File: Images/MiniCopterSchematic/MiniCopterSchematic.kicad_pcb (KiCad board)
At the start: 2 copper layers, 17 parts, among them M1 MOTOR_DC_1, M2 MOTOR_DC_2, M3 MOTOR_DC_3, M4 MOTOR_DC_4, Q1 FQP20NO6L, Q2 FQP20NO6L, Q3 FQP20NO6L, Q4 FQP20NO6L

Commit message: Working on PCB layout/wiring
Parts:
- added H1: MountingHole, MountingHole:MountingHole_3.2mm_M3, F.Cu at (166.4, 119.4)
- added H2: MountingHole, MountingHole:MountingHole_3.2mm_M3, F.Cu at (158.4, 111.4)
- added H3: MountingHole, MountingHole:MountingHole_3.2mm_M3, F.Cu at (158.4, 119.4)
- added H4: MountingHole, MountingHole:MountingHole_3.2mm_M3, F.Cu at (166.4, 111.4)
- IMU1: footprint Connector_PinSocket_2.54mm:PinSocket_1x07_P2.54mm_Vertical -> AA_Custom_Components:MPU6050
- moved M1 26.7 mm to (86.2, 123.8), turned to 0 degrees
- moved M4 17.8 mm to (97.0, 81.3), turned to 0 degrees
- moved LIPO_BATTERY_1 15.6 mm to (80.0, 92.2)
- moved Q1 14.9 mm to (97.7, 111.9)
- moved Q2 14.6 mm to (97.7, 116.7)
- moved M3 14.3 mm to (117.9, 81.3)
- moved LIPO_BATTERY_2 13.4 mm to (80.0, 110.6), turned to -90 degrees
- moved R3 12.3 mm to (113.0, 116.8)
- moved R4 12.3 mm to (113.0, 120.0)
- moved A1 11.7 mm to (110.2, 88.9)
- moved R1 11.1 mm to (113.0, 101.6)
- moved R2 11.1 mm to (113.0, 106.1)
- moved Q4 10.4 mm to (97.6, 126.5)
- moved IMU1 10.3 mm to (101.7, 87.7), turned to -90 degrees
- moved Q3 9.34 mm to (97.7, 121.5)
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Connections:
- IMU1 pad 1: unconnected-(IMU1-Pad1) -> +BATT
- IMU1 pad 2: unconnected-(IMU1-Pad2) -> GND
- IMU1 pad 3: SDA -> SCL
- IMU1 pad 4: SCL -> SDA
- IMU1 pad 6: GND -> unconnected-(IMU1-Pad6)
- IMU1 pad 7: +BATT -> unconnected-(IMU1-Pad7)
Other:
- board outline added: 76.2 x 55.9 mm

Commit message: Working on PCB
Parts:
- H1, H2, H3, H4: footprint MountingHole:MountingHole_3.2mm_M3 -> MountingHole:MountingHole_3.2mm_M3_Pad
- moved H1 95.6 mm to (78.7, 81.3)
- moved H3 80.0 mm to (78.7, 127.0)
- moved H2 32.1 mm to (145.4, 82.1)
- moved H4 26.6 mm to (144.8, 127.0)
- moved Q4 13.2 mm to (88.8, 116.7)
- moved Q3 13.2 mm to (88.9, 111.8)
- moved M1 8.91 mm to (95.1, 124.5)
- moved LIPO_BATTERY_1 1.91 mm to (80.0, 94.1)
- moved Q1 1.37 mm to (99.1, 111.8)
- moved Q2 1.37 mm to (99.1, 116.6)
- moved LIPO_BATTERY_2 1.27 mm to (80.0, 111.8)
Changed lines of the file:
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@@
   (net 36 "unconnected-(NRF24L01_1-Pad8)")
   (net 37 "unconnected-(IMU1-Pad8)")
-  (footprint "MountingHole:MountingHole_3.2mm_M3" (layer "F.Cu")
-    (at 166.37 119.38)
-    (descr "Mounting Hole 3.2mm, no annular, M3")
-    (tags "mounting hole 3.2mm no annular m3")
+  (footprint "MountingHole:MountingHole_3.2mm_M3_Pad" (layer "F.Cu")
+    (at 78.74 81.28)
+    (descr "Mounting Hole 3.2mm, M3")
+    (tags "mounting hole 3.2mm m3")
     (property "Sheetfile" "MiniCopterSchematic.kicad_sch")
     (property "Sheetname" "")
@@
     (fp_circle (center 0 0) (end 3.2 0) (layer "Cmts.User") (width 0.15) (fill none))
     (fp_circle (center 0 0) (end 3.45 0) (layer "F.CrtYd") (width 0.05) (fill none))
-    (pad "" np_thru_hole circle (at 0 0) (size 3.2 3.2) (drill 3.2) (layers *.Cu *.Mask))
+    (pad "1" thru_hole circle (at 0 0) (size 6.4 6.4) (drill 3.2) (layers *.Cu *.Mask))
   )
   (footprint "Connector_PinSocket_2.54mm:PinSocket_1x03_P2.54mm_Vertical" (layer "F.Cu")
-    (at 97.7095 121.532 90)
+    (at 88.9 111.76 90)
     (descr "Through hole straight socket strip, 1x03, 2.54mm pitch, single row (from Kicad 4.0.7), script generated")
     (tags "Through hole socket strip THT 1x03 2.54mm single row")
@@
   )
   (footprint "AA_Custom_Components:PowerPad_Pair_5.0x5.0mm" (layer "F.Cu")
-    (at 80.01 110.57 -90)
+    (at 80.01 111.84 -90)
     (descr "SMD rectangular pad as solderable power pads, square 5.0mm side length each")
     (tags "SMD pad rectangle square power")
@@
       (net 35 "Net-(M4-Pad2)") (pinfunction "-") (pintype "passive"))
   )
-  (footprint "MountingHole:MountingHole_3.2mm_M3" (layer "F.Cu")
-    (at 158.42 111.43)
-    (descr "Mounting Hole 3.2mm, no annular, M3")
-    (tags "mounting hole 3.2mm no annular m3")
+  (footprint "MountingHole:MountingHole_3.2mm_M3_Pad" (layer "F.Cu")
+    (at 145.43 82.09)
+    (descr "Mounting Hole 3.2mm, M3")
+    (tags "mounting hole 3.2mm m3")
     (property "Sheetfile" "MiniCopterSchematic.kicad_sch")
     (property "Sheetname" "")
@@
     (fp_circle (center 0 0) (end 3.2 0) (layer "Cmts.User") (width 0.15) (fill none))
     (fp_circle (center 0 0) (end 3.45 0) (layer "F.CrtYd") (width 0.05) (fill none))
-    (pad "" np_thru_hole circle (at 0 0) (size 3.2 3.2) (drill 3.2) (layers *.Cu *.Mask))
+    (pad "1" thru_hole circle (at 0 0) (size 6.4 6.4) (drill 3.2) (layers *.Cu *.Mask))
   )
   (footprint "AA_Custom_Components:PowerPad_Pair_4.0x4.0mm" (layer "F.Cu")
@@
       (net 33 "Net-(M2-Pad2)") (pinfunction "-") (pintype "passive"))
   )
-  (footprint "MountingHole:MountingHole_3.2mm_M3" (layer "F.Cu")
-    (at 166.37 111.43)
-    (descr "Mounting Hole 3.2mm, no annular, M3")
-    (tags "mounting hole 3.2mm no annular m3")
+  (footprint "MountingHole:MountingHole_3.2mm_M3_Pad" (layer "F.Cu")
+    (at 144.78 127)
+    (descr "Mounting Hole 3.2mm, M3")
+    (tags "mounting hole 3.2mm m3")
     (property "Sheetfile" "MiniCopterSchematic.kicad_sch")
     (property "Sheetname" "")
@@
     (fp_circle (center 0 0) (end 3.2 0) (layer "Cmts.User") (width 0.15) (fill none))
     (fp_circle (center 0 0) (end 3.45 0) (layer "F.CrtYd") (width 0.05) (fill none))
-    (pad "" np_thru_hole circle (at 0 0) (size 3.2 3.2) (drill 3.2) (layers *.Cu *.Mask))
+    (pad "1" thru_hole circle (at 0 0) (size 6.4 6.4) (drill 3.2) (layers *.Cu *.Mask))
   )
   (footprint "Connector_PinSocket_2.54mm:PinSocket_1x03_P2.54mm_Vertical" (layer "F.Cu")
-    (at 97.6945 111.905 90)
+    (at 99.06 111.76 90)
     (descr "Through hole straight socket strip, 1x03, 2.54mm pitch, single row (from Kicad 4.0.7), script generated")
     (tags "Through hole socket strip THT 1x03 2.54mm single row")
@@
   )
   (footprint "Connector_PinSocket_2.54mm:PinSocket_1x03_P2.54mm_Vertical" (layer "F.Cu")
-    (at 97.6945 116.731 90)
+    (at 99.06 116.586 90)
     (descr "Through hole straight socket strip, 1x03, 2.54mm pitch, single row (from Kicad 4.0.7), script generated")
     (tags "Through hole socket strip THT 1x03 2.54mm single row")
@@
   )
   (footprint "AA_Custom_Components:PowerPad_Pair_5.0x5.0mm" (layer "F.Cu")
-    (at 80.01 92.155 90)
+    (at 80.01 94.06 90)
     (descr "SMD rectangular pad as solderable power pads, square 5.0mm side length each")
     (tags "SMD pad rectangle square power")
@@
       (net 27 "+BATT") (pinfunction "-") (pintype "passive"))
   )
-  (footprint "MountingHole:MountingHole_3.2mm_M3" (layer "F.Cu")
-    (at 158.42 119.38)
-    (descr "Mounting Hole 3.2mm, no annular, M3")
-    (tags "mounting hole 3.2mm no annular m3")
+  (footprint "MountingHole:MountingHole_3.2mm_M3_Pad" (layer "F.Cu")
+    (at 78.74 127)
+    (descr "Mounting Hole 3.2mm, M3")
+    (tags "mounting hole 3.2mm m3")
     (property "Sheetfile" "MiniCopterSchematic.kicad_sch")
     (property "Sheetname" "")
@@
     (fp_circle (center 0 0) (end 3.2 0) (layer "Cmts.User") (width 0.15) (fill none))
     (fp_circle (center 0 0) (end 3.45 0) (layer "F.CrtYd") (width 0.05) (fill none))
-    (pad "" np_thru_hole circle (at 0 0) (size 3.2 3.2) (drill 3.2) (layers *.Cu *.Mask))
+    (pad "1" thru_hole circle (at 0 0) (size 6.4 6.4) (drill 3.2) (layers *.Cu *.Mask))
   )
   (footprint "Resistor_THT:R_Axial_DIN0207_L6.3mm_D2.5mm_P10.16mm_Horizontal" (layer "F.Cu")
@@
   )
   (footprint "AA_Custom_Components:PowerPad_Pair_4.0x4.0mm" (layer "F.Cu")
-    (at 86.17 123.825)
+    (at 95.06 124.46)
     (descr "SMD rectangular pad as solderable power pads, square 4.0mm side length each")
     (tags "SMD pad rectangle square power")
@@
   )
   (footprint "Connector_PinSocket_2.54mm:PinSocket_1x03_P2.54mm_Vertical" (layer "F.Cu")
-    (at 97.6425 126.461 90)
+    (at 88.833 116.689 90)
     (descr "Through hole straight socket strip, 1x03, 2.54mm pitch, single row (from Kicad 4.0.7), script generated")
     (tags "Through hole socket strip THT 1x03 2.54mm single row")

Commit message: Working on PCB
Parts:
- moved NRF24L01_1 4.07 mm to (139.8, 101.2)
- moved R1 3.76 mm to (112.6, 97.9)
- moved R2 3.76 mm to (112.6, 102.3)
- moved R3 3.76 mm to (112.6, 113.1)
- moved R4 3.15 mm to (112.7, 116.9)
- moved H2 2.11 mm to (145.7, 80.0)
- moved H1 1.28 mm to (78.7, 80.0)
- moved H4 0.96 mm to (145.7, 127.0)
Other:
- board size 76.2 x 55.9 mm -> 78.6 x 58.6 mm
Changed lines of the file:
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@@
   (net 37 "unconnected-(IMU1-Pad8)")
   (footprint "MountingHole:MountingHole_3.2mm_M3_Pad" (layer "F.Cu")
-    (at 78.74 81.28)
+    (at 78.74 80)
     (descr "Mounting Hole 3.2mm, M3")
     (tags "mounting hole 3.2mm m3")
@@
     (property "Sheetname" "")
     (attr exclude_from_pos_files)
-    (fp_text reference "H1" (at 0 -4.2) (layer "F.SilkS")
+    (fp_text reference "H1" (at 0 -4.2) (layer "F.Fab")
       (effects (font (size 1 1) (thickness 0.15)))
     )
@@
   )
   (footprint "Resistor_THT:R_Axial_DIN0207_L6.3mm_D2.5mm_P10.16mm_Horizontal" (layer "F.Cu")
-    (at 113.03 106.065)
+    (at 112.64 102.33)
     (descr "Resistor, Axial_DIN0207 series, Axial, Horizontal, pin pitch=10.16mm, 0.25W = 1/4W, length*diameter=6.3*2.5mm^2, http://cdn-reichelt.de/documents/datenblatt/B400/1_4W%23YAG.pdf")
     (tags "Resistor Axial_DIN0207 series Axial Horizontal pin pitch 10.16mm 0.25W = 1/4W length 6.3mm diameter 2.5mm")
@@
   )
   (footprint "AA_Custom_Components:NRF24L01_Breakout" (layer "F.Cu")
-    (at 139.831513 105.278487)
+    (at 139.836513 101.213487)
     (property "Sheetfile" "MiniCopterSchematic.kicad_sch")
     (property "Sheetname" "")
@@
       (effects (font (size 1 1) (thickness 0.15)))
     )
-    (fp_text value "ARDUINO NANO EVERY" (at 12.16 26.035 90) (layer "F.Fab")
+    (fp_text value "ARDUINO NANO EVERY" (at 11.83 22.9 90) (layer "F.Fab")
       (effects (font (size 1 1) (thickness 0.15)))
     )
@@
       (effects (font (size 1 1) (thickness 0.15)))
     )
-    (fp_text user "${REFERENCE}" (at 9.62 26.035 90) (layer "F.Fab")
+    (fp_text user "${REFERENCE}" (at 9.23 22.3 90) (layer "F.Fab")
       (effects (font (size 1 1) (thickness 0.15)))
     )
@@
   )
   (footprint "Resistor_THT:R_Axial_DIN0207_L6.3mm_D2.5mm_P10.16mm_Horizontal" (layer "F.Cu")
-    (at 113.03 120.015)
+    (at 112.7 116.88)
     (descr "Resistor, Axial_DIN0207 series, Axial, Horizontal, pin pitch=10.16mm, 0.25W = 1/4W, length*diameter=6.3*2.5mm^2, http://cdn-reichelt.de/documents/datenblatt/B400/1_4W%23YAG.pdf")
     (tags "Resistor Axial_DIN0207 series Axial Horizontal pin pitch 10.16mm 0.25W = 1/4W length 6.3mm diameter 2.5mm")
@@
   )
   (footprint "MountingHole:MountingHole_3.2mm_M3_Pad" (layer "F.Cu")
-    (at 145.43 82.09)
+    (at 145.74 80)
     (descr "Mounting Hole 3.2mm, M3")
     (tags "mounting hole 3.2mm m3")
@@
     (property "Sheetname" "")
     (attr exclude_from_pos_files)
-    (fp_text reference "H2" (at 0 -4.2) (layer "F.SilkS")
+    (fp_text reference "H2" (at 0 -4.2) (layer "F.Fab")
       (effects (font (size 1 1) (thickness 0.15)))
     )
@@
   )
   (footprint "MountingHole:MountingHole_3.2mm_M3_Pad" (layer "F.Cu")
-    (at 144.78 127)
+    (at 145.74 127)
     (descr "Mounting Hole 3.2mm, M3")
     (tags "mounting hole 3.2mm m3")
@@
     (property "Sheetname" "")
     (attr exclude_from_pos_files)
-    (fp_text reference "H4" (at 0 -4.2) (layer "F.SilkS")
+    (fp_text reference "H4" (at 0 -4.2) (layer "F.Fab")
       (effects (font (size 1 1) (thickness 0.15)))
     )
@@
     (property "Sheetname" "")
     (attr exclude_from_pos_files)
-    (fp_text reference "H3" (at 0 -4.2) (layer "F.SilkS")
+    (fp_text reference "H3" (at 0 -4.2) (layer "F.Fab")
       (effects (font (size 1 1) (thickness 0.15)))
     )
@@
   )
   (footprint "Resistor_THT:R_Axial_DIN0207_L6.3mm_D2.5mm_P10.16mm_Horizontal" (layer "F.Cu")
-    (at 113.03 101.62)
+    (at 112.64 97.885)
     (descr "Resistor, Axial_DIN0207 series, Axial, Horizontal, pin pitch=10.16mm, 0.25W = 1/4W, length*diameter=6.3*2.5mm^2, http://cdn-reichelt.de/documents/datenblatt/B400/1_4W%23YAG.pdf")
     (tags "Resistor Axial_DIN0207 series Axial Horizontal pin pitch 10.16mm 0.25W = 1/4W length 6.3mm diameter 2.5mm")
@@
   )
   (footprint "Resistor_THT:R_Axial_DIN0207_L6.3mm_D2.5mm_P10.16mm_Horizontal" (layer "F.Cu")
-    (at 113.03 116.84)
+    (at 112.64 113.105)
     (descr "Resistor, Axial_DIN0207 series, Axial, Horizontal, pin pitch=10.16mm, 0.25W = 1/4W, length*diameter=6.3*2.5mm^2, http://cdn-reichelt.de/documents/datenblatt/B400/1_4W%23YAG.pdf")
     (tags "Resistor Axial_DIN0207 series Axial Horizontal pin pitch 10.16mm 0.25W = 1/4W length 6.3mm diameter 2.5mm")
@@
     )
   )
-  (gr_line (start 149.86 132.08) (end 73.66 132.08) (layer "Edge.Cuts") (width 0.1))
-  (gr_line (start 149.86 76.2) (end 149.86 132.08) (layer "Edge.Cuts") (width 0.1))
-  (gr_line (start 73.66 76.2) (end 149.86 76.2) (layer "Edge.Cuts") (width 0.1))
-  (gr_line (start 73.66 132.08) (end 73.66 76.2) (layer "Edge.Cuts") (width 0.1))
+  (gr_line (start 78.8 132.8) (end 145.8 132.8) (layer "Edge.Cuts") (width 0.1))
+  (gr_arc (start 145.8 74.2) (mid 149.901219 75.898781) (end 151.6 80) (layer "Edge.Cuts") (width 0.1))
+  (gr_line (start 151.6 127) (end 151.6 80) (layer "Edge.Cuts") (width 0.1))
+  (gr_arc (start 73 80) (mid 74.698781 75.898781) (end 78.8 74.2) (layer "Edge.Cuts") (width 0.1))
+  (gr_arc (start 78.8 132.8) (mid 74.698781 131.101219) (end 73 127) (layer "Edge.Cuts") (width 0.1))
+  (gr_line (start 73 80) (end 73 127) (layer "Edge.Cuts") (width 0.1))
+  (gr_line (start 145.8 74.2) (end 78.8 74.2) (layer "Edge.Cuts") (width 0.1))
+  (gr_arc (start 151.6 127) (mid 149.901219 131.101219) (end 145.8 132.8) (layer "Edge.Cuts") (width 0.1))
+  (gr_rect (start 151.6 132.8) (end 73 74.25) (layer "User.2") (width 0.1) (fill none))
+  (dimension (type aligned) (layer "User.1")
+    (pts (xy 145.74 80) (xy 145.74 127))
+    (height -15.76)
+    (gr_text "47.0000 mm" (at 160.35 103.5 90) (layer "User.1")
+      (effects (font (size 1 1) (thickness 0.15)))
+    )
+    (format (units 3) (units_format 1) (precision 4))
+    (style (thickness 0.1) (arrow_length 1.27) (text_position_mode 0) (extension_height 0.58642) (extension_offset 0.5) keep_text_aligned)
+  )
+  (dimension (type aligned) (layer "User.1")
+    (pts (xy 78.74 127) (xy 145.74 127))
+    (height 12)
+    (gr_text "67.0000 mm" (at 112.24 137.85) (layer "User.1")
+      (effects (font (size 1 1) (thickness 0.15)))
+    )
+    (format (units 3) (units_format 1) (precision 4))
+    (style (thickness 0.1) (arrow_length 1.27) (text_position_mode 0) (extension_height 0.58642) (extension_offset 0.5) keep_text_aligned)
+  )
+  (dimension (type aligned) (layer "User.1")
+    (pts (xy 151.5 127) (xy 151.5 132.75))
+    (height -0.099999)
+    (gr_text "5.7500 mm" (at 150.449999 129.875 90) (layer "User.1")
+      (effects (font (size 1 1) (thickness 0.15)))
+    )
+    (format (units 3) (units_format 1) (precision 4))
+    (style (thickness 0.1) (arrow_length 1.27) (text_position_mode 0) (extension_height 0.58642) (extension_offset 0.5) keep_text_aligned)
+  )
+  (dimension (type aligned) (layer "User.1")
+    (pts (xy 78.74 127) (xy 78.74 80))
+    (height -12.74)
+    (gr_text "47.0000 mm" (at 64.85 103.5 90) (layer "User.1")
+      (effects (font (size 1 1) (thickness 0.15)))
+    )
+    (format (units 3) (units_format 1) (precision 4))
+    (style (thickness 0.1) (arrow_length 1.27) (text_position_mode 0) (extension_height 0.58642) (extension_offset 0.5) keep_text_aligned)
+  )
+  (dimension (type aligned) (layer "User.1")
+    (pts (xy 78.74 80) (xy 73 80))
+    (height 0)
+    (gr_text "5.7400 mm" (at 75.87 78.85) (layer "User.1")
+      (effects (font (size 1 1) (thickness 0.15)))
+    )
+    (format (units 3) (units_format 1) (precision 4))
+    (style (thickness 0.1) (arrow_length 1.27) (text_position_mode 0) (extension_height 0.58642) (extension_offset 0.5) keep_text_aligned)
+  )
+  (dimension (type aligned) (layer "User.1")
+    (pts (xy 73 80) (xy 73 74.25))
+    (height 0)
+    (gr_text "5.7500 mm" (at 71.85 77.125 90) (layer "User.1")
+      (effects (font (size 1 1) (thickness 0.15)))
+    )
+    (format (units 3) (units_format 1) (precision 4))
+    (style (thickness 0.1) (arrow_length 1.27) (text_position_mode 0) (extension_height 0.58642) (extension_offset 0.5) keep_text_aligned)
+  )
+  (dimension (type aligned) (layer "User.1")
+    (pts (xy 145.74 127) (xy 151.5 127))
+    (height 0)
+    (gr_text "5.7600 mm" (at 148.62 125.85) (layer "User.1")
+      (effects (font (size 1 1) (thickness 0.15)))
+    )
+    (format (units 3) (units_format 1) (precision 4))
+    (style (thickness 0.1) (arrow_length 1.27) (text_position_mode 0) (extension_height 0.58642) (extension_offset 0.5) keep_text_aligned)
+  )
+  (dimension (type aligned) (layer "User.1")
+    (pts (xy 145.74 80) (xy 78.74 80))
+    (height 12.5)
+    (gr_text "67.0000 mm" (at 112.24 66.35) (layer "User.1")
+      (effects (font (size 1 1) (thickness 0.15)))
+    )
+    (format (units 3) (units_format 1) (precision 4))
+    (style (thickness 0.1) (arrow_length 1.27) (text_position_mode 0) (extension_height 0.58642) (extension_offset 0.5) keep_text_aligned)
+  )
+  (group "" (id 2a93e3a3-b881-49ef-867e-a1a44b3351e0)
+    (members
+      02191e1c-6e9e-4a43-9f98-f563d88a889a
+      91ff1f66-ea32-4789-87d9-a31fccfb0c90
+      a6a59a31-77eb-4f13-af83-01d5d082f3a7
+      c2671e34-1237-4f64-867d-81a1e491b10b
+    )
+  )
 )

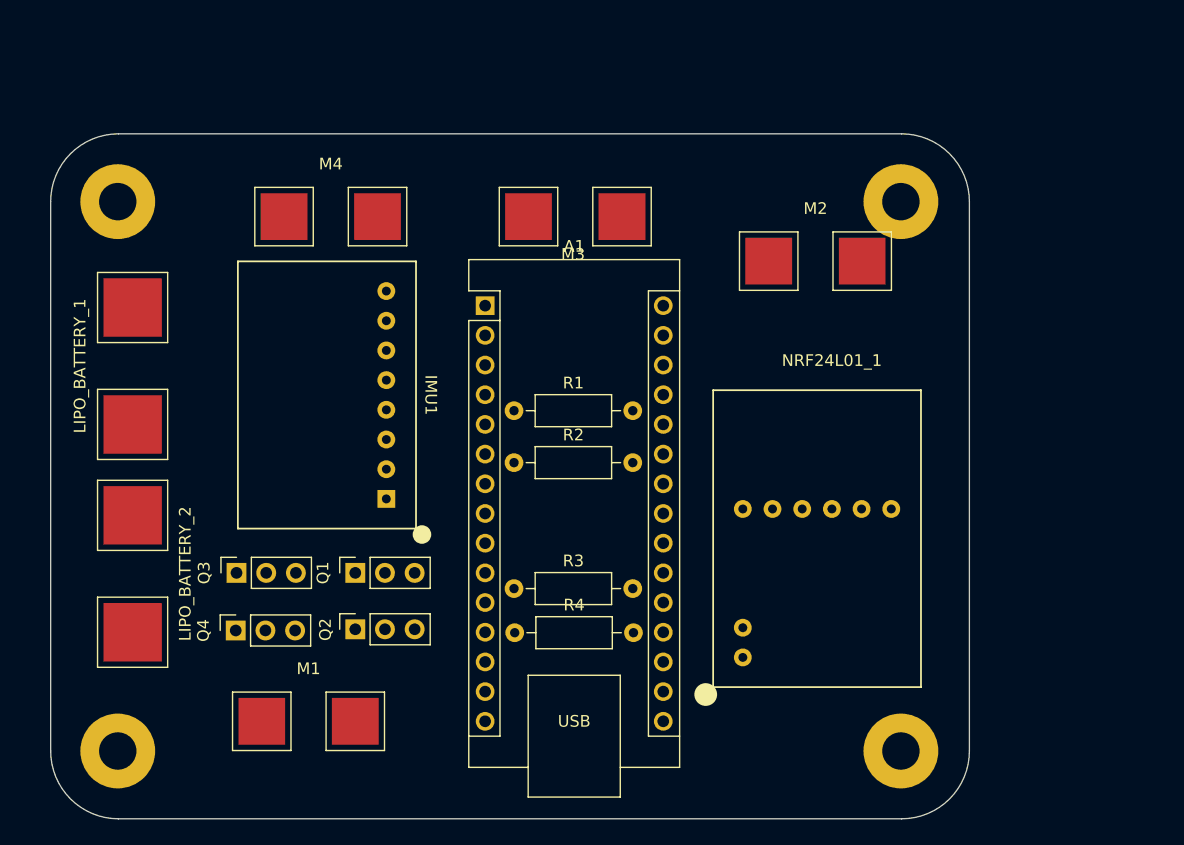
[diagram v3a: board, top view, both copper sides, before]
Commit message: Fixing layout of components on PCB
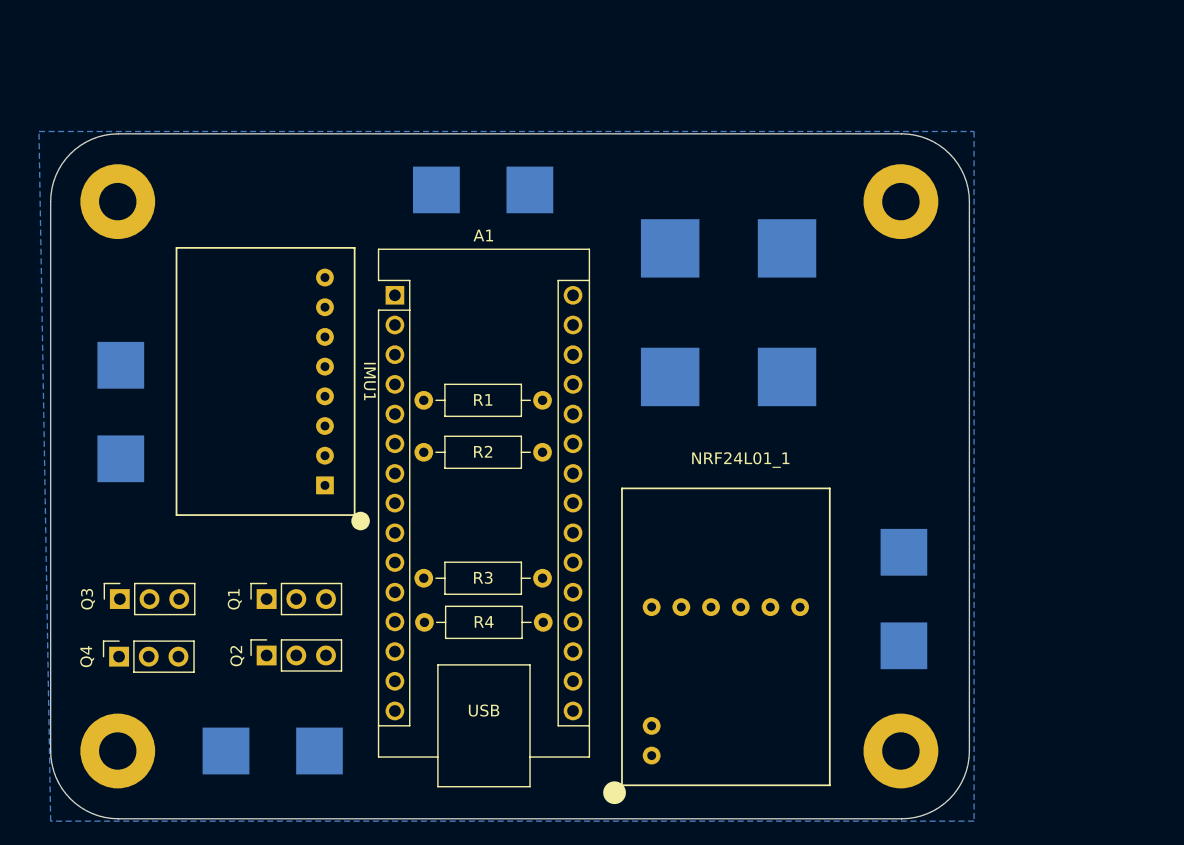
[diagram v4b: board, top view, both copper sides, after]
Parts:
- LIPO_BATTERY_1, LIPO_BATTERY_2, M1, M2, M3, M4: moved to B.Cu
- moved LIPO_BATTERY_2 58.1 mm to (131.0, 84.0), turned to 0 degrees
- moved LIPO_BATTERY_1 51.0 mm to (131.0, 95.0), turned to 0 degrees
- moved M2 29.9 mm to (146.0, 114.0), turned to 90 degrees
- moved M4 24.5 mm to (79.0, 98.0), turned to -90 degrees
- moved NRF24L01_1 11.5 mm to (132.0, 109.6)
- moved Q4 10.2 mm to (78.9, 118.9)
- moved Q3 10.2 mm to (78.9, 114.0)
- moved M3 8.20 mm to (110.0, 79.0)
- moved Q1 7.91 mm to (91.5, 114.0)
- moved Q2 7.91 mm to (91.5, 118.8)
- moved A1 7.77 mm to (102.5, 88.0)
- moved R1 7.77 mm to (104.9, 97.0)
- moved R2 7.77 mm to (104.9, 101.4)
- moved R3 7.77 mm to (104.9, 112.2)
- moved R4 7.77 mm to (105.0, 116.0)
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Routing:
- added copper zone on B.Cu, net GND
